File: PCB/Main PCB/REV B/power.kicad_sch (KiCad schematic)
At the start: 14 parts, among them U5 AMS1117-3.3, U6 TPS2115APWR

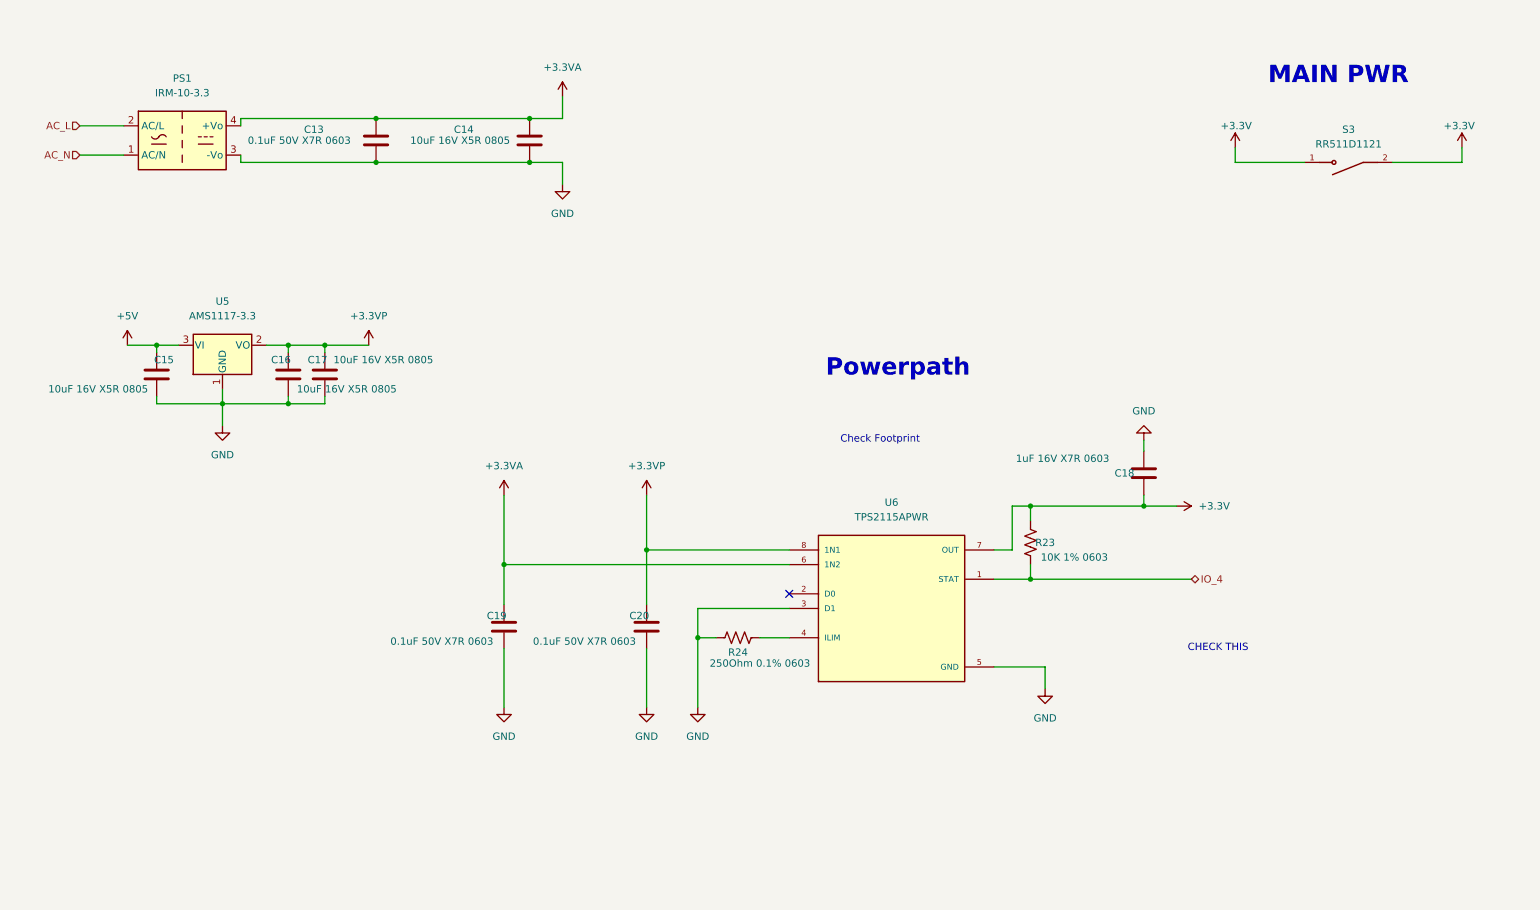
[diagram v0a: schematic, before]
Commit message: PCB schematic updates, added 5V power supply
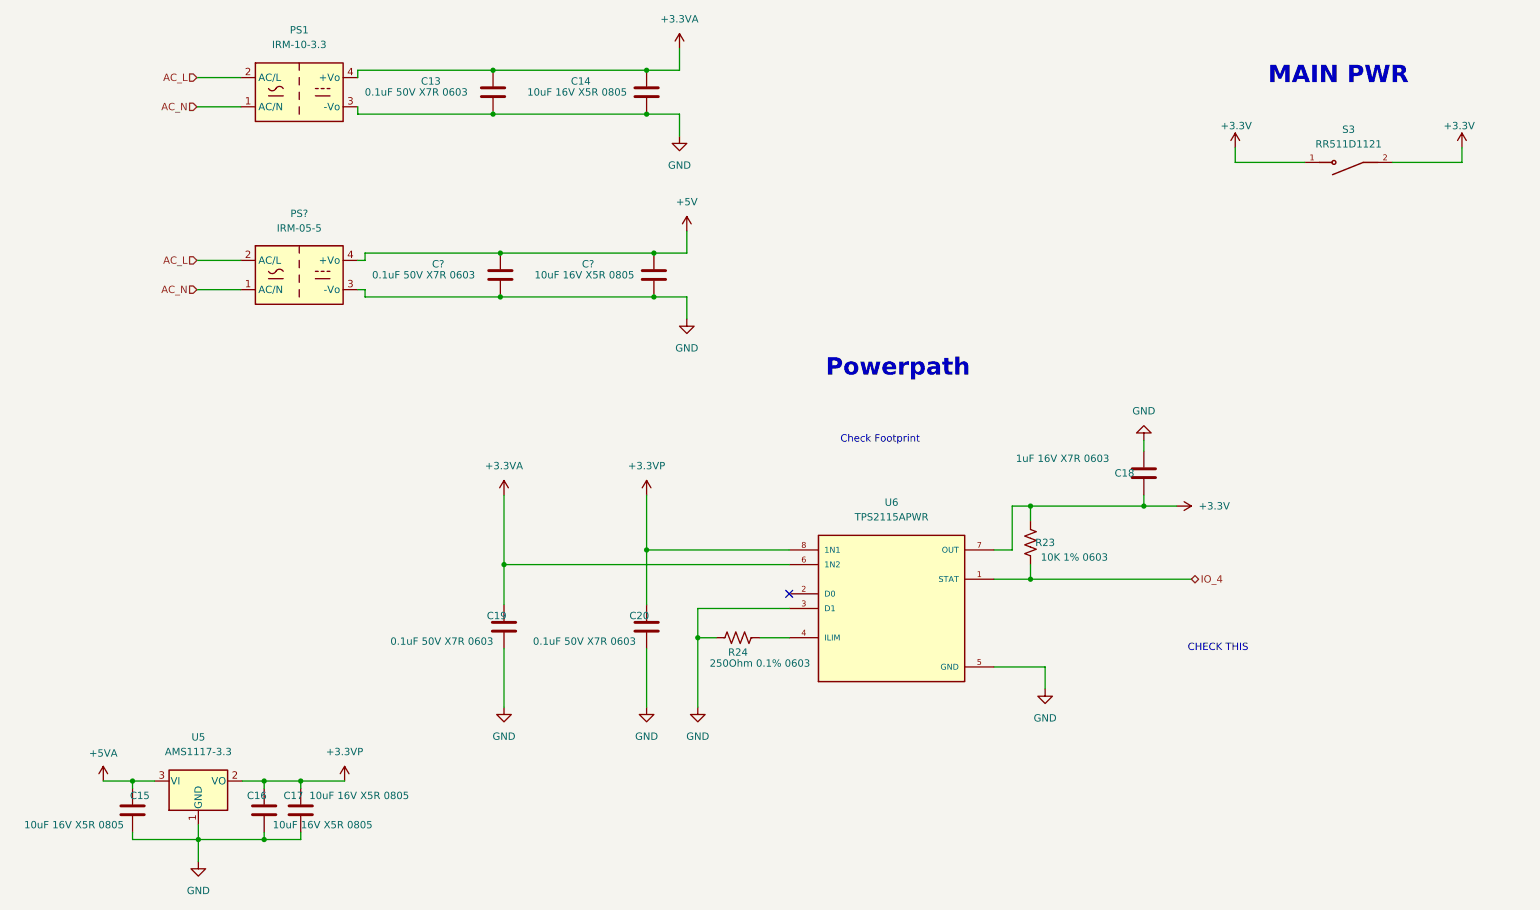
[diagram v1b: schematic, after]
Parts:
- added C?: 10uF 16V X5R 0805, Capacitor_SMD:C_0805_2012Metric, symbol Device:C
- added C?: 0.1uF 50V X7R 0603, Capacitor_SMD:C_0603_1608Metric, symbol Device:C
- added PS?: IRM-05-5, Converter_ACDC:Converter_ACDC_MeanWell_IRM-05-xx_THT, symbol Converter_ACDC:IRM-05-5
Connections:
- net +5V: now also C?.1, C?.2, PS?.4 (+Vo); no longer C15.1, U5.3 (VI)
- net AC_L: now also PS?.2 (AC/L)
- net AC_N: now also PS?.1 (AC/N)
- net GND: now also C?.1, C?.2, PS?.3 (-Vo)
- new net +5VA: C15.1, U5.3 (VI)
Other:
- moved on the sheet: C13, C14, C15, C16, C17, PS1, U5

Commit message: PCB schematic updates, Modified and fixed all power sheets
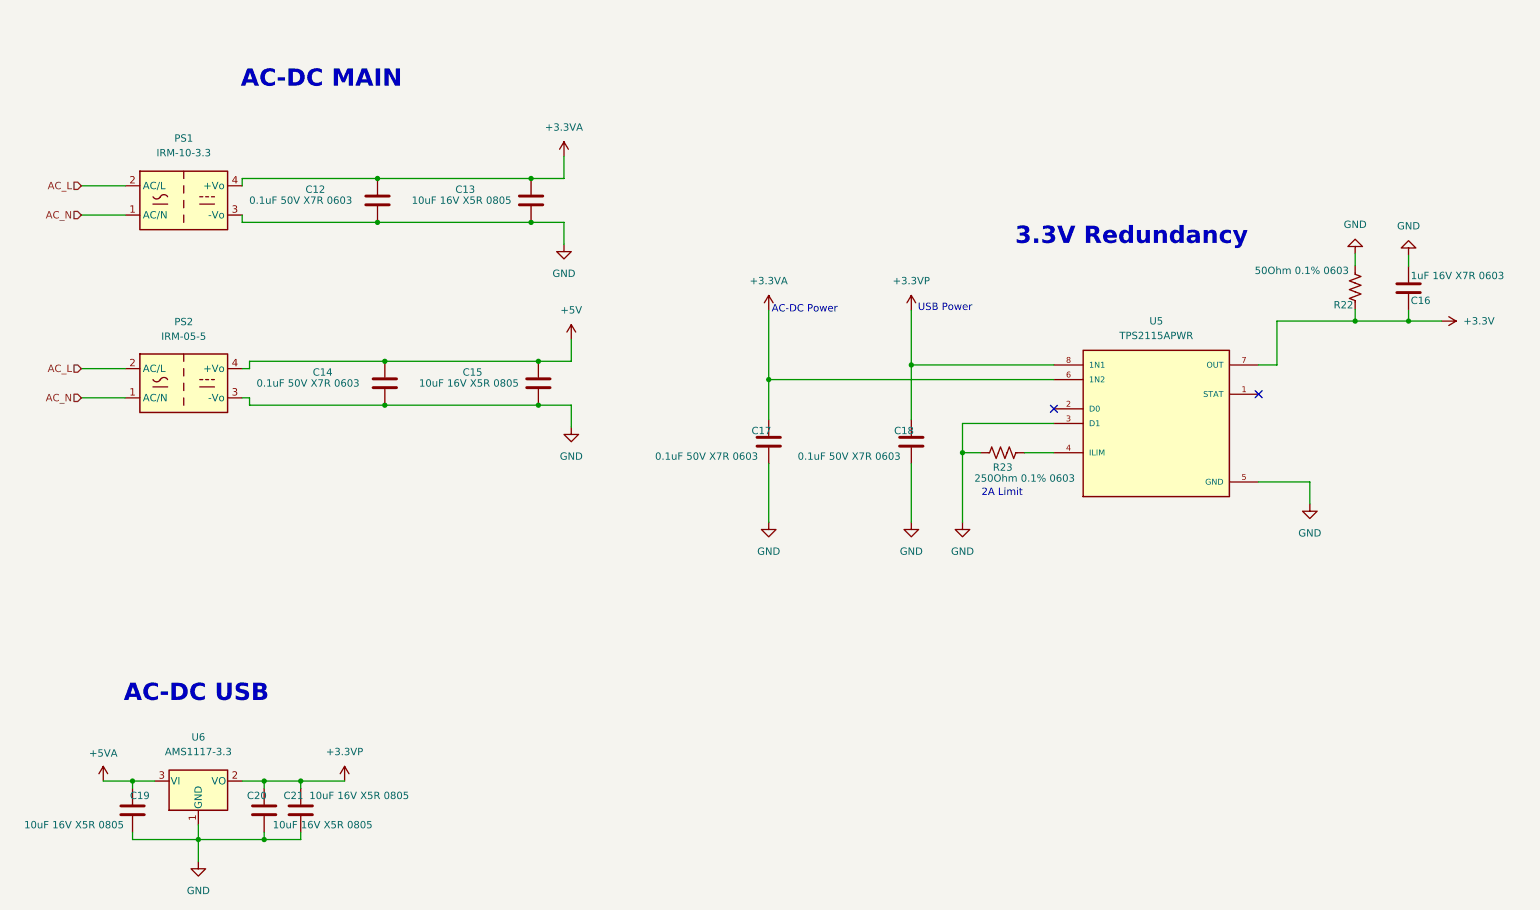
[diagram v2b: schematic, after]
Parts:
- removed R23: 10K 1% 0603, Resistor_SMD:R_0603_1608Metric, symbol Device:R_US
- removed S3: RR511D1121, Customs Smoker:E-SWITCH_RR511D1121, symbol RR511D1121:RR511D1121
- added R22: 50Ohm 0.1% 0603, Resistor_SMD:R_0603_1608Metric, symbol Device:R_US
- U5: renamed from U6; footprint Customs Smoker:SOP65P640X120-8N -> Customs Smoker:PW8-M
- gave numbers to parts that had none: 3
- renumbered C13 to C12, C14 to C13, C18 to C16, C19 to C17, C20 to C18, C15 to C19, C16 to C20, C17 to C21, R24 to R23, U5 to U6
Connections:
- net +3.3V: now also R22.2
- net GND: now also R22.1
- net IO_4: no longer names the net of U5.1 (STAT)
- no-connect marks 1 -> 2
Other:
- note added: "2A Limit"
- note added: "3.3V Redundancy"
- note added: "AC-DC MAIN"
- note added: "AC-DC Power"
- note added: "AC-DC USB"
- note added: "USB Power"
- note removed: "CHECK THIS"
- note removed: "Check Footprint"
- note removed: "MAIN PWR"
- note removed: "Powerpath"
- moved on the sheet: C12, C13, C14, C15, C16, C17, C18, PS1, PS2, R23, U5

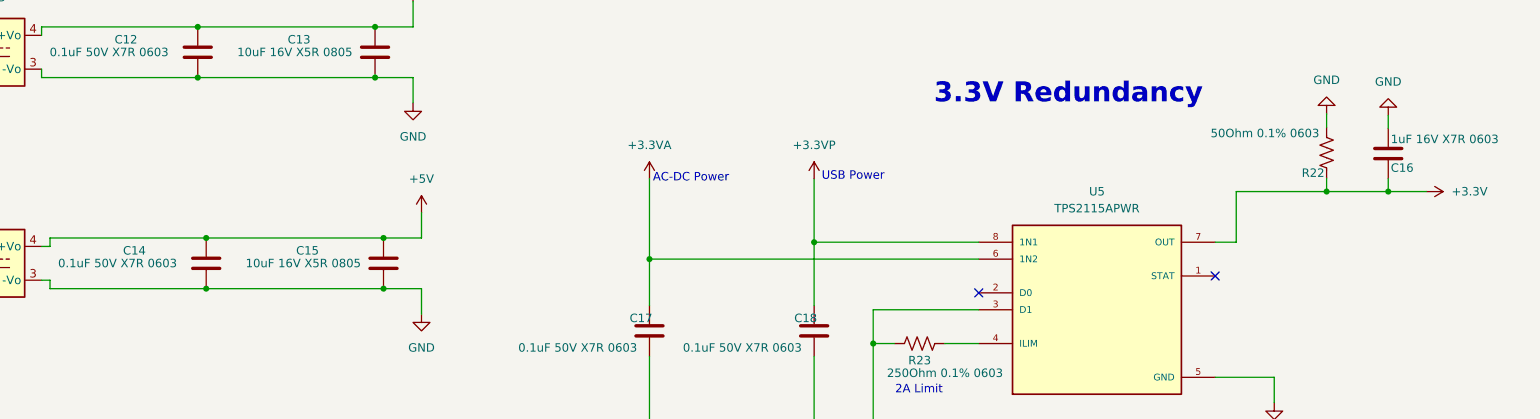
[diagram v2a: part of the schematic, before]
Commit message: PCB schematic updates, Find mosfet for relay on circuit
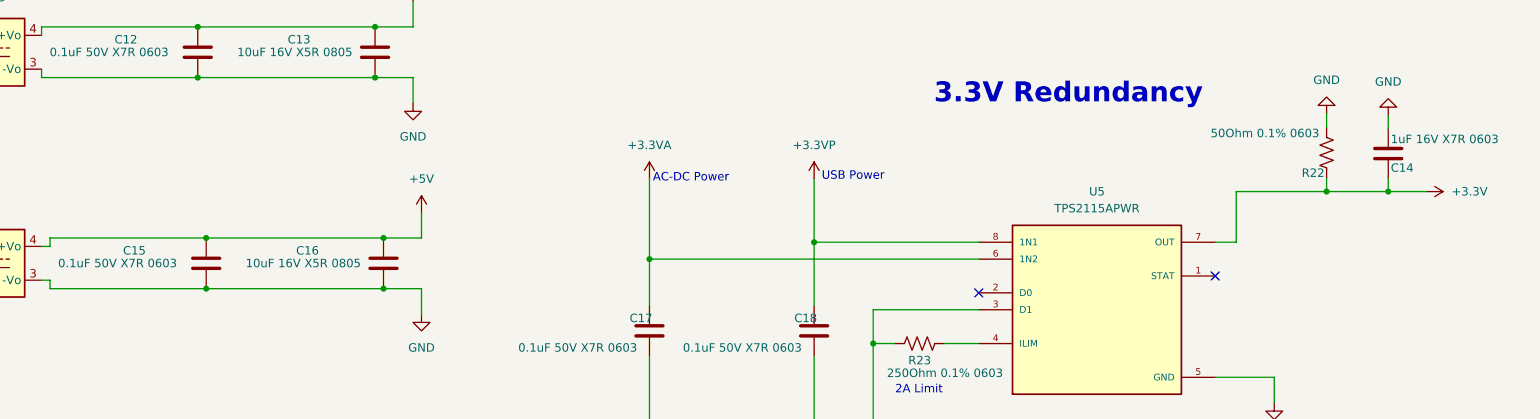
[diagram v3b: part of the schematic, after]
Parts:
- renumbered C16 to C14, C14 to C15, C15 to C16
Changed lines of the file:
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@@
   (symbol (lib_id "Device:C") (at 111.379 85.344 0) (mirror y) (unit 1)
     (in_bom yes) (on_board yes)
-    (property "Reference" "C15" (id 0) (at 99.949 83.439 0))
+    (property "Reference" "C16" (id 0) (at 99.949 83.439 0))
     (property "Value" "10uF 16V X5R 0805" (id 1) (at 99.314 85.344 0))
     (property "Footprint" "Capacitor_SMD:C_0805_2012Metric" (id 2) (at 110.4138 89.154 0)
@@
   (symbol (lib_id "power:+3.3VP") (at 176.149 72.644 0) (unit 1)
     (in_bom yes) (on_board yes) (fields_autoplaced)
-    (property "Reference" "#PWR060" (id 0) (at 179.959 73.914 0)
+    (property "Reference" "#PWR058" (id 0) (at 179.959 73.914 0)
       (effects (font (size 1.27 1.27)) hide)
     )
@@
   (symbol (lib_id "power:+3.3V") (at 268.224 74.549 270) (unit 1)
     (in_bom yes) (on_board yes) (fields_autoplaced)
-    (property "Reference" "#PWR061" (id 0) (at 264.414 74.549 0)
+    (property "Reference" "#PWR059" (id 0) (at 264.414 74.549 0)
       (effects (font (size 1.27 1.27)) hide)
     )
@@
   (symbol (lib_id "power:GND") (at 117.094 92.964 0) (unit 1)
     (in_bom yes) (on_board yes)
-    (property "Reference" "#PWR056" (id 0) (at 117.094 99.314 0)
+    (property "Reference" "#PWR061" (id 0) (at 117.094 99.314 0)
       (effects (font (size 1.27 1.27)) hide)
     )
@@
   (symbol (lib_id "power:+3.3VA") (at 151.384 72.644 0) (unit 1)
     (in_bom yes) (on_board yes) (fields_autoplaced)
-    (property "Reference" "#PWR059" (id 0) (at 151.384 76.454 0)
+    (property "Reference" "#PWR057" (id 0) (at 151.384 76.454 0)
       (effects (font (size 1.27 1.27)) hide)
     )
@@
   (symbol (lib_id "power:GND") (at 253.238 62.865 180) (unit 1)
     (in_bom yes) (on_board yes) (fields_autoplaced)
-    (property "Reference" "#PWR057" (id 0) (at 253.238 56.515 0)
+    (property "Reference" "#PWR055" (id 0) (at 253.238 56.515 0)
       (effects (font (size 1.27 1.27)) hide)
     )
@@
   (symbol (lib_id "Device:C") (at 84.709 85.344 0) (mirror x) (unit 1)
     (in_bom yes) (on_board yes)
-    (property "Reference" "C14" (id 0) (at 73.914 83.439 0))
+    (property "Reference" "C15" (id 0) (at 73.914 83.439 0))
     (property "Value" "0.1uF 50V X7R 0603" (id 1) (at 71.374 85.344 0))
     (property "Footprint" "Capacitor_SMD:C_0603_1608Metric" (id 2) (at 85.6742 81.534 0)
@@
   (symbol (lib_id "power:GND") (at 262.509 63.119 180) (unit 1)
     (in_bom yes) (on_board yes) (fields_autoplaced)
-    (property "Reference" "#PWR058" (id 0) (at 262.509 56.769 0)
+    (property "Reference" "#PWR056" (id 0) (at 262.509 56.769 0)
       (effects (font (size 1.27 1.27)) hide)
     )
@@
   (symbol (lib_id "power:+5V") (at 117.094 77.724 0) (unit 1)
     (in_bom yes) (on_board yes) (fields_autoplaced)
-    (property "Reference" "#PWR055" (id 0) (at 117.094 81.534 0)
+    (property "Reference" "#PWR060" (id 0) (at 117.094 81.534 0)
       (effects (font (size 1.27 1.27)) hide)
     )
@@
   (symbol (lib_id "Device:C") (at 262.509 68.834 0) (unit 1)
     (in_bom yes) (on_board yes)
-    (property "Reference" "C16" (id 0) (at 262.89 70.993 0)
+    (property "Reference" "C14" (id 0) (at 262.89 70.993 0)
       (effects (font (size 1.27 1.27)) (justify left))
     )
